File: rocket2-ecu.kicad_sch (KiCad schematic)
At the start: 26 parts, among them J1 ALARM, J24 XT60, P3 PAD_SMD, P4 PAD_SMD, Q1 DMG3402L, U1 BMI088, U2 MS560702BA03-50, U3 BMM350, U4 GC-XPORT-ENH

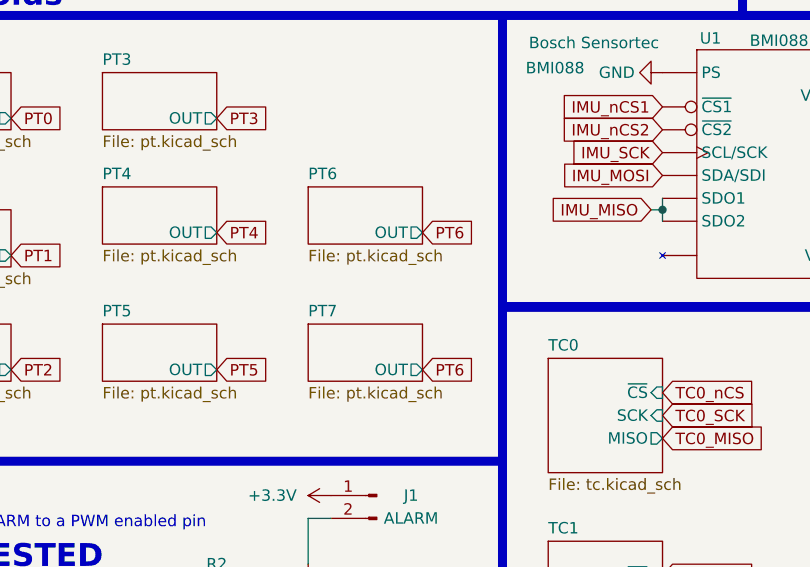
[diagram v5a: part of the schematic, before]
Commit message: 3/4 DC-DC converters done
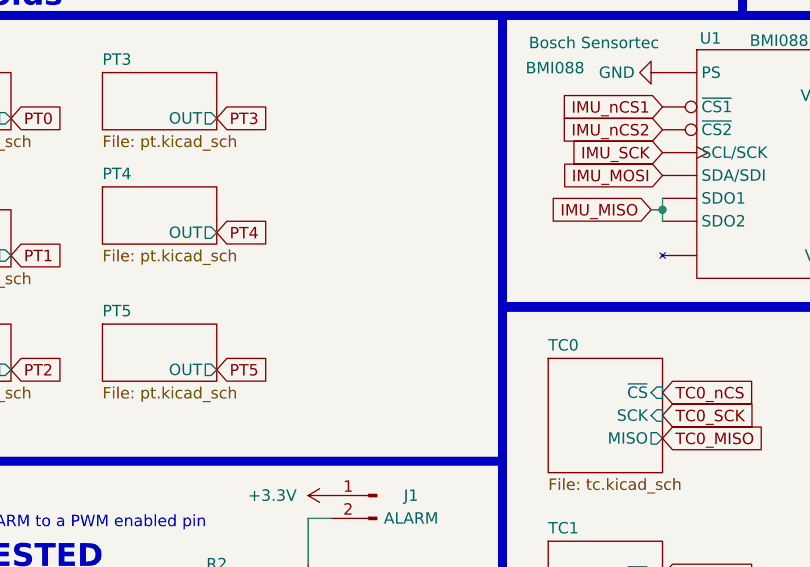
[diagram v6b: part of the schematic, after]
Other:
- removed sheet PT6
- removed sheet PT7
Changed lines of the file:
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@@
 		)
 	)
-	(global_label "PT6"
-		(shape input)
-		(at 73.66 142.24 0)
-		(fields_autoplaced yes)
-		(effects
-			(font
-				(size 1.27 1.27)
-			)
-			(justify left)
-		)
-		(property "Intersheetrefs" "${INTERSHEET_REFS}"
-			(at 80.0923 142.24 0)
-			(effects
-				(font
-					(size 1.27 1.27)
-				)
-				(justify left)
-				(hide yes)
-			)
-		)
-	)
 	(global_label "PT2"
 		(shape input)
@@
 		)
 	)
-	(global_label "PT6"
-		(shape input)
-		(at 73.66 157.48 0)
-		(fields_autoplaced yes)
-		(effects
-			(font
-				(size 1.27 1.27)
-			)
-			(justify left)
-		)
-		(property "Intersheetrefs" "${INTERSHEET_REFS}"
-			(at 80.0923 157.48 0)
-			(effects
-				(font
-					(size 1.27 1.27)
-				)
-				(justify left)
-				(hide yes)
-			)
-		)
-	)
 	(global_label "TC1_nCS"
 		(shape input)
@@
 	)
 	(sheet
-		(at 60.96 137.16)
-		(size 12.7 6.35)
-		(exclude_from_sim no)
-		(in_bom yes)
-		(on_board yes)
-		(dnp no)
-		(fields_autoplaced yes)
-		(stroke
-			(width 0.1524)
-			(type solid)
-		)
-		(fill
-			(color 0 0 0 0.0000)
-		)
-		(property "Sheetname" "PT6"
-			(at 60.96 136.4484 0)
-			(effects
-				(font
-					(size 1.27 1.27)
-				)
-				(justify left bottom)
-			)
-		)
-		(property "Sheetfile" "pt.kicad_sch"
-			(at 60.96 144.0946 0)
-			(effects
-				(font
-					(size 1.27 1.27)
-				)
-				(justify left top)
-			)
-		)
-		(pin "OUT" output
-			(at 73.66 142.24 0)
-			(effects
-				(font
-					(size 1.27 1.27)
-				)
-				(justify right)
-			)
-		)
-		(instances
-			(project "rocket2-ecu"
-				(path "/02606b2c-b376-4ffb-9781-f9cea3f70994"
-					(page "24")
-				)
-			)
-		)
-	)
-	(sheet
 		(at 38.1 137.16)
 		(size 12.7 6.35)
@@
 				)
 			)
-		)
-	)
-	(sheet
-		(at 60.96 152.4)
-		(size 12.7 6.35)
-		(exclude_from_sim no)
-		(in_bom yes)
-		(on_board yes)
-		(dnp no)
-		(fields_autoplaced yes)
-		(stroke
-			(width 0.1524)
-			(type solid)
-		)
-		(fill
-			(color 0 0 0 0.0000)
-		)
-		(property "Sheetname" "PT7"
-			(at 60.96 151.6884 0)
-			(effects
-				(font
-					(size 1.27 1.27)
-				)
-				(justify left bottom)
-			)
-		)
-		(property "Sheetfile" "pt.kicad_sch"
-			(at 60.96 159.3346 0)
-			(effects
-				(font
-					(size 1.27 1.27)
-				)
-				(justify left top)
-			)
-		)
-		(pin "OUT" output
-			(at 73.66 157.48 0)
-			(effects
-				(font
-					(size 1.27 1.27)
-				)
-				(justify right)
-			)
-		)
-		(instances
-			(project "rocket2-ecu"
-				(path "/02606b2c-b376-4ffb-9781-f9cea3f70994"
-					(page "26")
-				)
-			)

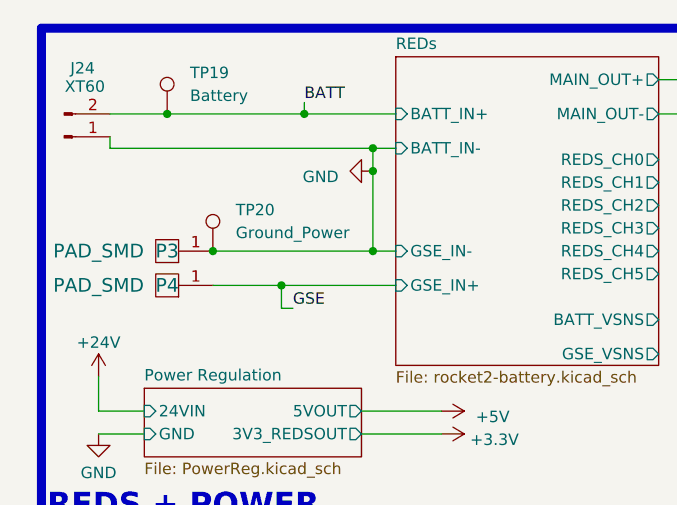
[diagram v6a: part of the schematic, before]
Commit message: power connectors done
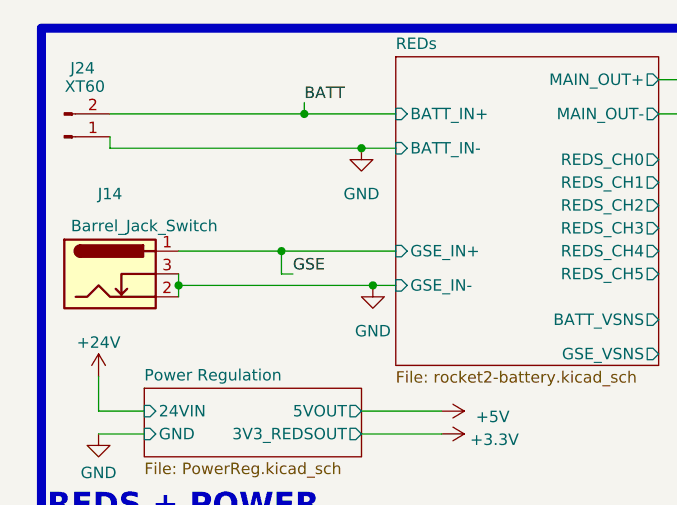
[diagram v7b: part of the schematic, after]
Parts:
- removed P3, P4: PAD_SMD, TestPoint:TestPoint_Plated_Hole_D4.0mm, symbol pkl_misc:PAD_SMD
- removed TP19: Battery, TestPoint:TestPoint_Plated_Hole_D2.0mm, symbol Connector:TestPoint
- removed TP20: Ground_Power, TestPoint:TestPoint_Plated_Hole_D2.0mm, symbol Connector:TestPoint
- added J14: Barrel_Jack_Switch, Connector_BarrelJack:BarrelJack_Horizontal, symbol Connector:Barrel_Jack_Switch
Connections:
- net GND: now also J14.2, J14.3
- net GSE: now also J14.1

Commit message: ALMOST
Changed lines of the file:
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@@
+		)
+	)
+	(global_label "REDs_CH0"
+		(shape input)
+		(at 81.28 26.67 0)
+		(fields_autoplaced yes)
+		(effects
+			(font
+				(size 1.27 1.27)
+			)
+			(justify left)
+		)
+		(property "Intersheetrefs" "${INTERSHEET_REFS}"
+			(at 93.7599 26.67 0)
+			(effects
+				(font
+					(size 1.27 1.27)
+				)
+				(justify left)
+				(hide yes)
+			)
 		)
 	)
@@
 		)
 	)
+	(global_label "REDs_CH3"
+		(shape input)
+		(at 81.28 34.29 0)
+		(fields_autoplaced yes)
+		(effects
+			(font
+				(size 1.27 1.27)
+			)
+			(justify left)
+		)
+		(property "Intersheetrefs" "${INTERSHEET_REFS}"
+			(at 93.7599 34.29 0)
+			(effects
+				(font
+					(size 1.27 1.27)
+				)
+				(justify left)
+				(hide yes)
+			)
+		)
+	)
 	(global_label "TC0_SCK"
 		(shape input)
@@
 		)
 	)
+	(global_label "REDs_CH1"
+		(shape input)
+		(at 81.28 29.21 0)
+		(fields_autoplaced yes)
+		(effects
+			(font
+				(size 1.27 1.27)
+			)
+			(justify left)
+		)
+		(property "Intersheetrefs" "${INTERSHEET_REFS}"
+			(at 93.7599 29.21 0)
+			(effects
+				(font
+					(size 1.27 1.27)
+				)
+				(justify left)
+				(hide yes)
+			)
+		)
+	)
 	(global_label "ALT_nCS"
 		(shape input)
@@
 		)
 	)
+	(global_label "REDs_CH5"
+		(shape input)
+		(at 81.28 39.37 0)
+		(fields_autoplaced yes)
+		(effects
+			(font
+				(size 1.27 1.27)
+			)
+			(justify left)
+		)
+		(property "Intersheetrefs" "${INTERSHEET_REFS}"
+			(at 93.7599 39.37 0)
+			(effects
+				(font
+					(size 1.27 1.27)
+				)
+				(justify left)
+				(hide yes)
+			)
+		)
+	)
 	(global_label "IMU_nCS2"
 		(shape input)
@@
 		)
 	)
+	(global_label "ECU_BV"
+		(shape input)
+		(at 81.28 44.45 0)
+		(fields_autoplaced yes)
+		(effects
+			(font
+				(size 1.27 1.27)
+			)
+			(justify left)
+		)
+		(property "Intersheetrefs" "${INTERSHEET_REFS}"
+			(at 91.3409 44.45 0)
+			(effects
+				(font
+					(size 1.27 1.27)
+				)
+				(justify left)
+				(hide yes)
+			)
+		)
+	)
 	(global_label "MAG_SCL"
 		(shape input)
@@
 		)
 	)
+	(global_label "REDs_CH2"
+		(shape input)
+		(at 81.28 31.75 0)
+		(fields_autoplaced yes)
+		(effects
+			(font
+				(size 1.27 1.27)
+			)
+			(justify left)
+		)
+		(property "Intersheetrefs" "${INTERSHEET_REFS}"
+			(at 93.7599 31.75 0)
+			(effects
+				(font
+					(size 1.27 1.27)
+				)
+				(justify left)
+				(hide yes)
+			)
+		)
+	)
 	(global_label "ALARM"
 		(shape input)
@@
 		)
 	)
-	(global_label "SOLENOID3_EN"
+	(global_label "SOLENOID4_EN"
 		(shape input)
 		(at 91.44 101.6 0)
@@
 		)
 		(property "Intersheetrefs" "${INTERSHEET_REFS}"
-			(at 108.2553 101.6 0)
+			(at 108.3347 101.6 0)
 			(effects
 				(font
@@
 		)
 	)
+	(global_label "ECU_GS"
+		(shape input)
+		(at 81.28 48.26 0)
+		(fields_autoplaced yes)
+		(effects
+			(font
+				(size 1.27 1.27)
+			)
+			(justify left)
+		)
+		(property "Intersheetrefs" "${INTERSHEET_REFS}"
+			(at 91.4618 48.26 0)
+			(effects
+				(font
+					(size 1.27 1.27)
+				)
+				(justify left)
+				(hide yes)
+			)
+		)
+	)
 	(global_label "MAG_SDA"
 		(shape input)
@@
 		)
 	)
-	(global_label "SOLENOID3_FB"
+	(global_label "SOLENOID4_FB"
 		(shape input)
 		(at 91.44 107.95 0)
@@
 		)
 		(property "Intersheetrefs" "${INTERSHEET_REFS}"
-			(at 108.1344 107.95 0)
+			(at 108.2138 107.95 0)
 			(effects
 				(font
@@
 			(effects
 				(font
+					(size 1.27 1.27)
+				)
+				(justify left)
+				(hide yes)
+			)
+		)
+	)
+	(global_label "REDs_CH4"
+		(shape input)
+		(at 81.28 36.83 0)
+		(fields_autoplaced yes)
+		(effects
+			(font
+				(size 1.27 1.27)
+			)
+			(justify left)
+		)
+		(property "Intersheetrefs" "${INTERSHEET_REFS}"
+			(at 93.7599 36.83 0)
+			(effects
+				(font
